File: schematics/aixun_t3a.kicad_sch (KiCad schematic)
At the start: 90 parts, among them P3 Debug, P4 GX12-5, Q1 PNP, Q1 Q_NPN_BEC, Q3 AO4413, Q4 Q_NPN_BEC, SW1 SET, SW2 CH, U1 MY240H2416S-V2, U2 GD32F303RCT6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

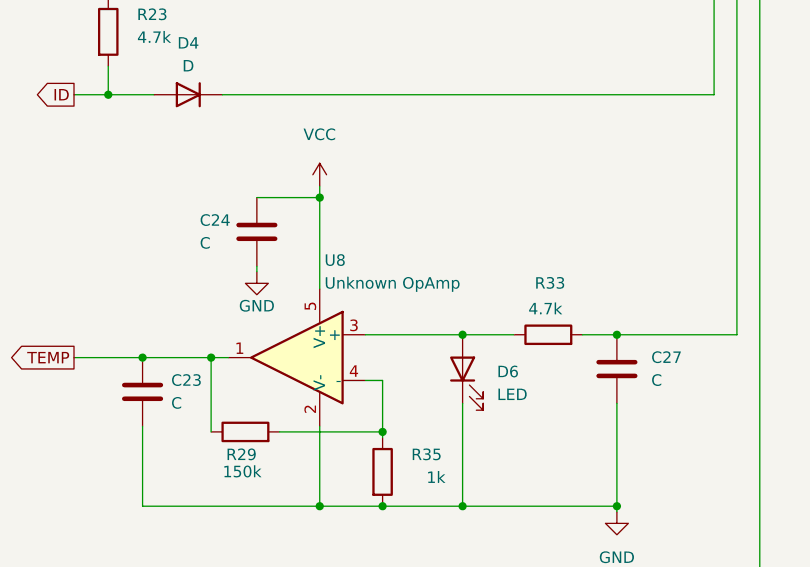
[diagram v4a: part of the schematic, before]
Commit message: schematics: Update opamp
It's a 3PEAK TP1541A

Signed-off-by: Michael Niewöhner <foss@mniewoehner.de>
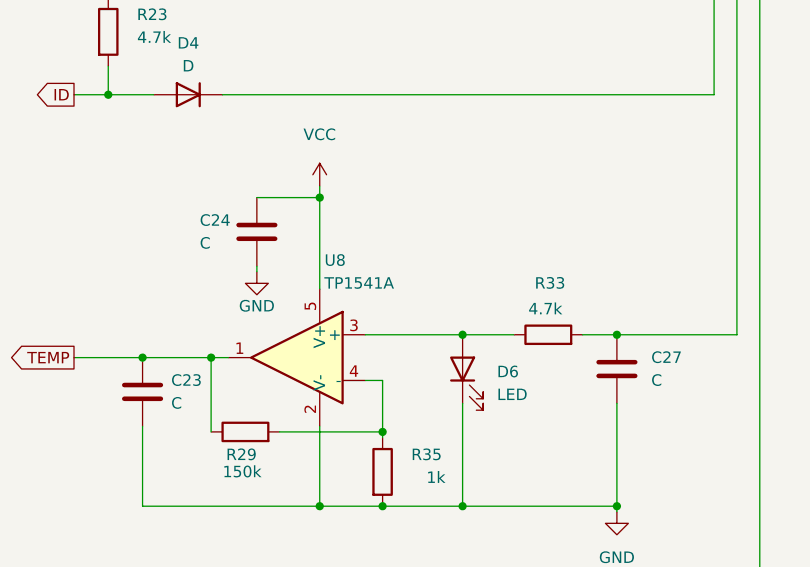
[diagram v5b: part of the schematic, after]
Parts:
- U8: value Unknown OpAmp -> TP1541A
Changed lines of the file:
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@@
       (effects (font (size 1.27 1.27)) (justify right))
     )
-    (property "Value" "Unknown OpAmp" (id 1) (at 328.1806 165.735 0)
+    (property "Value" "TP1541A" (id 1) (at 328.1806 165.735 0)
       (effects (font (size 1.27 1.27)) (justify right))
     )
@@
       (effects (font (size 1.27 1.27)) (justify left) hide)
     )
-    (property "Datasheet" "" (id 3) (at 325.12 168.91 0)
+    (property "Datasheet" "https://datasheet.lcsc.com/szlcsc/3PEAK-TP1542A-SR_C99005.pdf" (id 3) (at 325.12 168.91 0)
       (effects (font (size 1.27 1.27)) hide)
     )
@@
     )
     (path "/aebf913b-fb12-4a9a-9570-d7dae9c27b17"
-      (reference "U8") (unit 1) (value "Unknown OpAmp") (footprint "Package_TO_SOT_SMD:SOT-23-5")
+      (reference "U8") (unit 1) (value "TP1541A") (footprint "Package_TO_SOT_SMD:SOT-23-5")
     )
     (path "/2f60ff9a-62d9-41d1-a1f9-e1489881141b"
